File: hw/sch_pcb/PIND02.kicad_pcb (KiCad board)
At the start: 2 copper layers, 60.5 x 40.1 mm, 58 parts, among them J1 Conn_Coaxial, J2 MLAB I2C interface, J3 HEADER_2x01, M1 HOLE M3, M2 HOLE M3, M3 HOLE, M4 HOLE, M5 RFShield_TwoPieces, Q1 2SK2394-6, U1 OPA2314, U2 ISL21080DIH312Z-TK, U3 SHT31-DIS, U4 TPS613222ADBV

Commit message: Routed PCB.
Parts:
- D1: value BZV55C-5,6V -> BZV55C-6,2V; footprint Diode_SMD:D_SMA -> Diode_SMD:D_MiniMELF
- moved R2 5.74 mm to (142.0, 94.2), turned to 90 degrees
- moved C6 3.59 mm to (141.5, 99.7), turned to 180 degrees
- moved D1 1.92 mm to (123.1, 109.2), turned to 180 degrees
- moved C7 1.70 mm to (140.8, 97.4), turned to 180 degrees
- moved R9 1.57 mm to (142.5, 107.0), turned to 90 degrees
- moved C3 1.49 mm to (151.4, 111.0)
- moved C14 1.14 mm to (167.3, 99.2)
- moved R11 1.02 mm to (140.4, 107.0)
- moved R7 0.69 mm to (136.1, 115.3)
- moved C4 0.65 mm to (154.0, 112.0)
- moved C11 0.64 mm to (136.1, 113.0)
- moved C2 0.64 mm to (129.4, 119.6)
- moved C10 0.52 mm to (136.6, 110.6)
- moved R6 0.46 mm to (135.2, 107.5)
- moved R3 0.40 mm to (145.3, 111.7)
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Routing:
- net GND: track 13.7 -> 16.8 mm, vias 10 -> 12
- net /REF: track 52.4 -> 50.7 mm
- net Net-(U1B-V+): track 6.27 -> 7.78 mm
- net GNDA: track 36.8 -> 35.4 mm, vias 6 -> 3
- net Net-(U1B-+): track 10.9 -> 12.1 mm
- net Net-(J1-In): track 6.75 -> 7.89 mm
- net Net-(U1B--): track 5.99 -> 7.12 mm
- net Net-(C14-Pad2): track 31.7 -> 30.7 mm
- net Net-(C21-Pad1): track 5.65 -> 6.16 mm
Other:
- board text added: "DC ENABLE"
- board text added: "SIGNAL OUT DC IN"
- board text removed: "OUT"
- board text removed: "Signal+Bias"

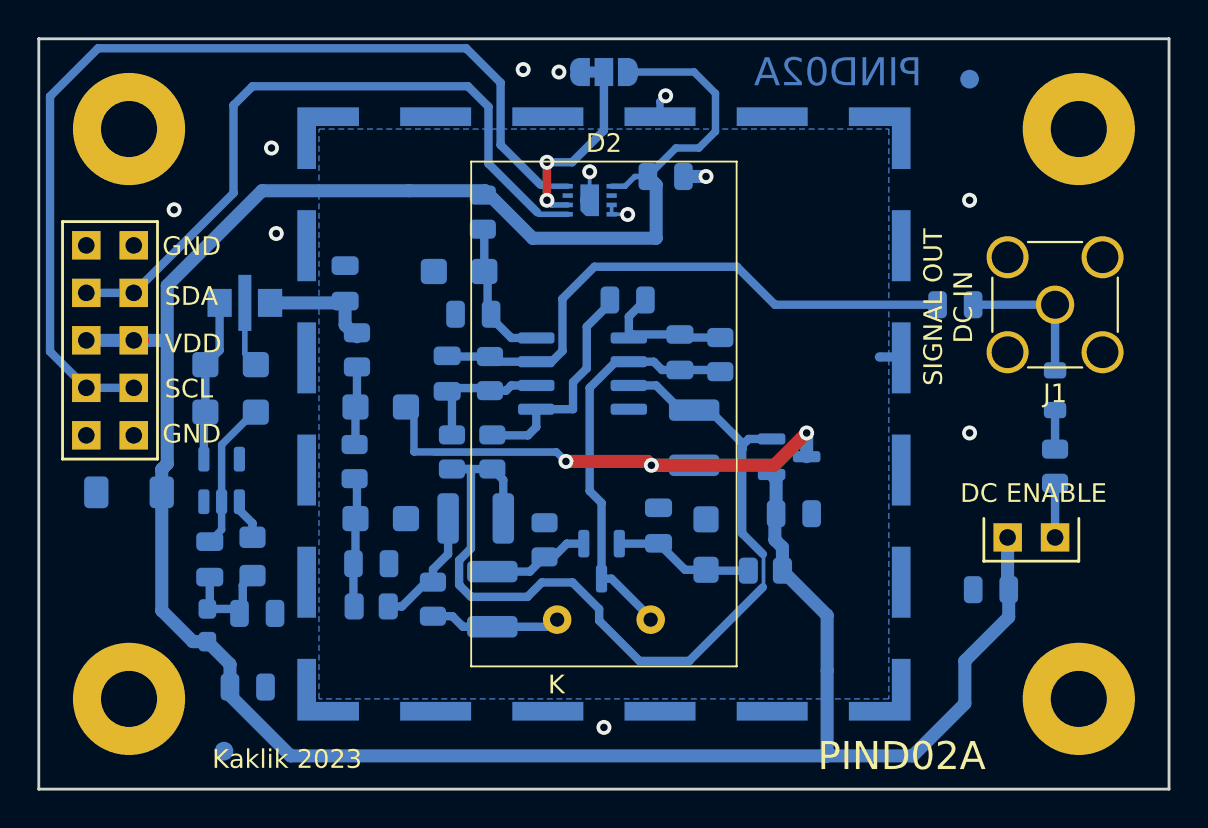
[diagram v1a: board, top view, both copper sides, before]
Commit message: Add solder mask keepout zone. Resolve #1.
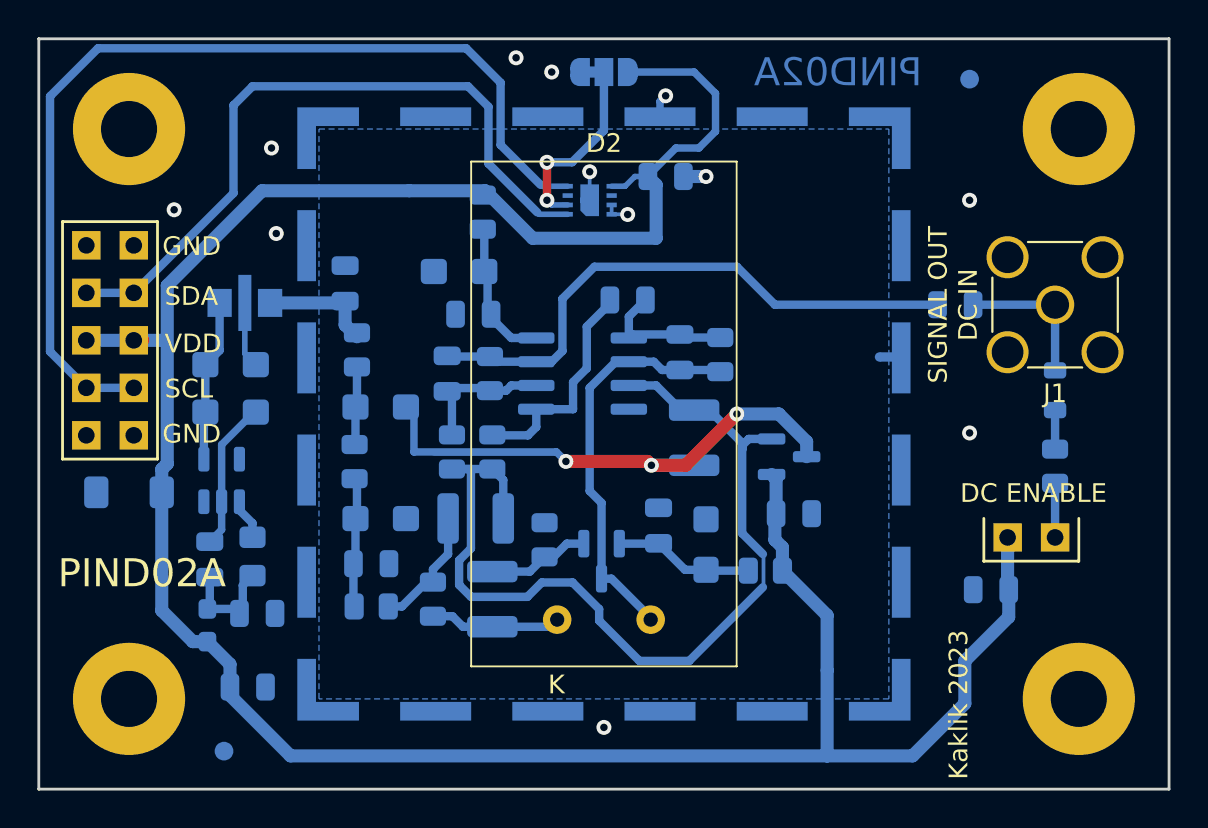
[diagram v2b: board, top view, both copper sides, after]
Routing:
- net GNDA: track 35.4 -> 36.0 mm
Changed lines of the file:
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@@
     (effects (font (size 1 1) (thickness 0.127)) (justify left bottom))
   )
-  (gr_text "SIGNAL OUT\nDC IN" (at 168.312 99.285 90) (layer "F.SilkS")
+  (gr_text "SIGNAL OUT\nDC IN" (at 168.566 99.158 90) (layer "F.SilkS")
     (effects (font (size 1 1) (thickness 0.127)) (justify bottom))
   )
-  (gr_text "Kaklik 2023" (at 127.545 124.05) (layer "F.SilkS")
+  (gr_text "Kaklik 2023" (at 168.058 124.558 90) (layer "F.SilkS")
     (effects (font (size 1 1) (thickness 0.127)) (justify left bottom))
   )
-  (gr_text "PIND02A" (at 159.93 124.177) (layer "F.SilkS")
+  (gr_text "PIND02A" (at 119.29 114.398) (layer "F.SilkS")
     (effects (font (size 1.5 1.5) (thickness 0.127)) (justify left bottom))
   )
@@
   (segment (start 134.561 99.061) (end 134.657 98.965) (width 0.7) (layer "B.Cu") (net 1))
   (via (at 151.802 87.982) (size 0.8) (drill 0.4) (layers "F.Cu" "B.Cu") (net 2))
-  (via (at 146.094 86.712002) (size 0.8) (drill 0.4) (layers "F.Cu" "B.Cu") (net 2))
+  (via (at 145.706 86.712002) (size 0.8) (drill 0.4) (layers "F.Cu" "B.Cu") (net 2))
   (via (at 168.058 106.016) (size 0.8) (drill 0.4) (layers "F.Cu" "B.Cu") (net 2))
   (via (at 153.961 92.3) (size 0.8) (drill 0.4) (layers "F.Cu" "B.Cu") (net 2))
   (via (at 168.058 93.57) (size 0.8) (drill 0.4) (layers "F.Cu" "B.Cu") (net 2))
-  (via (at 144.182 86.578) (size 0.8) (drill 0.4) (layers "F.Cu" "B.Cu") (net 2))
+  (via (at 143.801 85.95) (size 0.8) (drill 0.4) (layers "F.Cu" "B.Cu") (net 2))
   (via (at 125.513 94.078) (size 0.8) (drill 0.4) (layers "F.Cu" "B.Cu") (net 2))
   (via (at 149.77 94.332) (size 0.8) (drill 0.4) (layers "F.Cu" "B.Cu") (net 2))
@@
   (segment (start 143.117 108.5305) (end 142.531 107.9445) (width 0.45) (layer "B.Cu") (net 13))
   (segment (start 155.896 106.687) (end 156.247 106.336) (width 0.45) (layer "B.Cu") (net 13))
-  (segment (start 155.896 106.62) (end 155.896 106.554) (width 0.45) (layer "B.Cu") (net 13))
   (segment (start 153.064594 118.208) (end 150.397957 118.208) (width 0.45) (layer "B.Cu") (net 13))
-  (segment (start 155.896 106.62) (end 155.896 106.905) (width 0.45) (layer "B.Cu") (net 13))
   (segment (start 145.176957 114.013) (end 144.407957 114.782) (width 0.45) (layer "B.Cu") (net 13))
+  (segment (start 155.896 106.554) (end 154.137 104.795) (width 0.45) (layer "B.Cu") (net 13))
   (segment (start 143.117 110.588) (end 142.994406 110.588) (width 0.45) (layer "B.Cu") (net 13))
   (segment (start 149.832 103.476) (end 151.294 103.476) (width 0.45) (layer "B.Cu") (net 13))
@@
   (segment (start 146.823043 114.013) (end 145.176957 114.013) (width 0.45) (layer "B.Cu") (net 13))
   (segment (start 157.005297 114.267297) (end 153.064594 118.208) (width 0.45) (layer "B.Cu") (net 13))
-  (segment (start 155.896 106.554) (end 154.137 104.795) (width 0.45) (layer "B.Cu") (net 13))
   (segment (start 152.613 104.795) (end 153.326 104.795) (width 0.45) (layer "B.Cu") (net 13))
+  (segment (start 155.896 106.905) (end 155.896 106.554) (width 0.45) (layer "B.Cu") (net 13))
   (segment (start 150.397957 118.208) (end 148.246 116.056043) (width 0.45) (layer "B.Cu") (net 13))
   (segment (start 151.294 103.476) (end 152.613 104.795) (width 0.45) (layer "B.Cu") (net 13))
   (segment (start 141.394 114.782) (end 140.756 114.144) (width 0.45) (layer "B.Cu") (net 13))
   (segment (start 140.756 112.826406) (end 141.388 112.194406) (width 0.45) (layer "B.Cu") (net 13))
-  (segment (start 154.137 104.795) (end 153.326 104.795) (width 0.45) (layer "B.Cu") (net 13))
   (segment (start 148.246 115.435957) (end 146.823043 114.013) (width 0.45) (layer "B.Cu") (net 13))
   (segment (start 141.388 107.9445) (end 140.372 107.9445) (width 0.45) (layer "B.Cu") (net 13))
@@
   (segment (start 157.036 112.527406) (end 157.036 114.236594) (width 0.2) (layer "B.Cu") (net 13))
   (segment (start 148.246 116.056043) (end 148.246 115.435957) (width 0.45) (layer "B.Cu") (net 13))
+  (segment (start 154.137 104.795) (end 153.326 104.795) (width 0.45) (layer "B.Cu") (net 13))
   (segment (start 144.407957 114.782) (end 141.394 114.782) (width 0.45) (layer "B.Cu") (net 13))
   (segment (start 146.849 103.297173) (end 147.582 102.564173) (width 0.45) (layer "B.Cu") (net 14))
@@
   (segment (start 172.630001 106.881499) (end 172.63 106.8815) (width 0.45) (layer "B.Cu") (net 25))
   (segment (start 172.630001 104.7925) (end 172.630001 106.881499) (width 0.45) (layer "B.Cu") (net 25))
-  (segment (start 157.61449 107.745) (end 159.3435 106.01599) (width 0.7) (layer "F.Cu") (net 30))
+  (segment (start 151.04 107.745) (end 152.867 107.745) (width 0.7) (layer "F.Cu") (net 30))
   (segment (start 150.835 107.54) (end 151.04 107.745) (width 0.7) (layer "F.Cu") (net 30))
   (segment (start 146.468 107.54) (end 150.835 107.54) (width 0.7) (layer "F.Cu") (net 30))
-  (segment (start 151.04 107.745) (end 157.61449 107.745) (width 0.7) (layer "F.Cu") (net 30))
+  (segment (start 152.867 107.745) (end 155.611988 105.000012) (width 0.7) (layer "F.Cu") (net 30))
+  (segment (start 155.611988 105.000012) (end 155.611988 105) (width 0.7) (layer "F.Cu") (net 30))
   (via (at 151.04 107.745) (size 0.8) (drill 0.4) (layers "F.Cu" "B.Cu") (net 30))
-  (via (at 159.3435 106.01599) (size 0.8) (drill 0.4) (layers "F.Cu" "B.Cu") (net 30))
+  (via (at 155.611988 105) (size 0.8) (drill 0.4) (layers "F.Cu" "B.Cu") (net 30))
   (via (at 146.468 107.54) (size 0.8) (drill 0.4) (layers "F.Cu" "B.Cu") (net 30))
   (segment (start 153.326 107.745) (end 151.04 107.745) (width 0.7) (layer "B.Cu") (net 30))
-  (segment (start 159.3435 107.286) (end 159.3435 106.01599) (width 0.7) (layer "B.Cu") (net 30))
   (segment (start 138.34 107.032) (end 138.34 105.055) (width 0.4) (layer "B.Cu") (net 30))
   (segment (start 146.468 107.54) (end 146.01 107.082) (width 0.3) (layer "B.Cu") (net 30))
+  (segment (start 157.859949 105) (end 155.611988 105) (width 0.7) (layer "B.Cu") (net 30))
+  (segment (start 159.3435 106.483551) (end 157.859949 105) (width 0.7) (layer "B.Cu") (net 30))
   (segment (start 146.01 107.082) (end 139.406 107.082) (width 0.3) (layer "B.Cu") (net 30))
   (segment (start 146.468 107.54) (end 145.96 107.032) (width 0.4) (layer "B.Cu") (net 30))
+  (segment (start 159.3435 107.286) (end 159.3435 106.483551) (width 0.7) (layer "B.Cu") (net 30))
   (segment (start 145.96 107.032) (end 138.34 107.032) (width 0.4) (layer "B.Cu") (net 30))
   (segment (start 138.34 105.055) (end 137.912 104.627) (width 0.4) (layer "B.Cu") (net 30))
@@
       )
     )
+  )
+  (zone (net 0) (net_name "") (layer "F.Mask") (hatch full 0.508)
+    (connect_pads (clearance 0.2))
+    (min_thickness 0.101) (filled_areas_thickness no)
+    (fill yes (thermal_gap 0.508) (thermal_bridge_width 0.508))
+    (polygon
+      (pts
+        (xy 165.518 125.094893)
+        (xy 131.482 125.092247)
+        (xy 131.482 84.934)
+        (xy 165.518 84.934)
+      )
+    )

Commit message: Kontrola a upravy pred vyrobou
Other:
- rule pad_to_mask_clearance: 0 -> 0.2
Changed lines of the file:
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@@
       (dielectric_constraints no)
     )
-    (pad_to_mask_clearance 0)
+    (pad_to_mask_clearance 0.2)
     (aux_axis_origin 112.94 130.4)
     (grid_origin 112.94 130.4)
